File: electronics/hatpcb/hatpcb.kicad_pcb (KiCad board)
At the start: 2 copper layers, 72 x 60 mm, 4 parts, among them J1 Raspberry_Pi_GPIO, J2 encoder_1, J3 encoder_2, J4 Motor_Driver

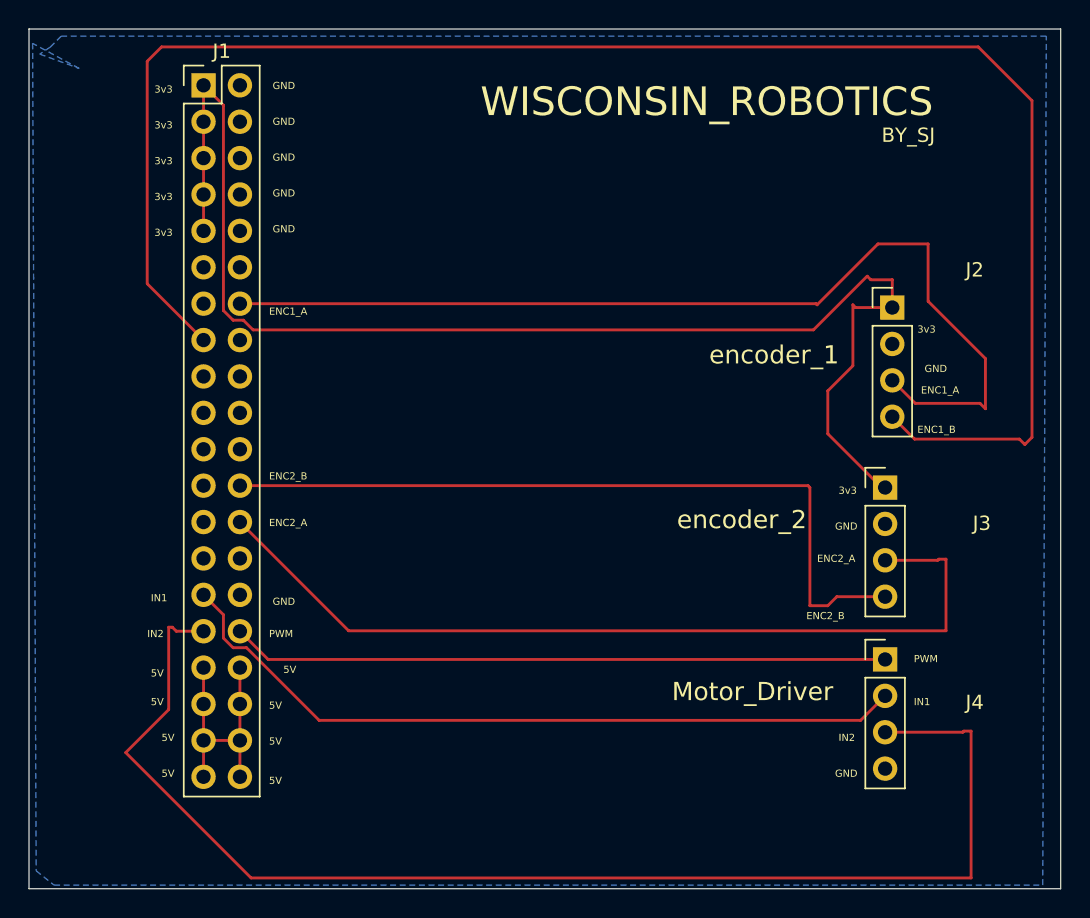
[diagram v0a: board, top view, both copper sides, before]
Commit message: Update hatpcb routing
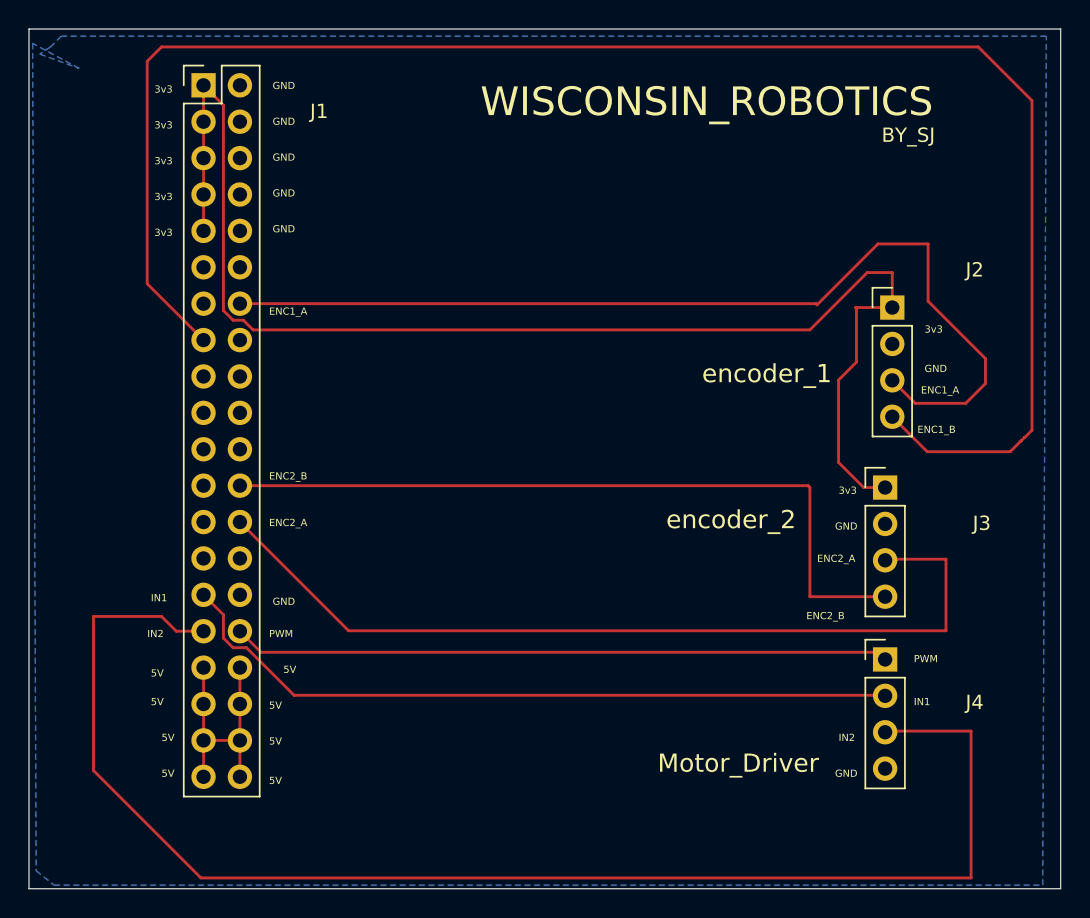
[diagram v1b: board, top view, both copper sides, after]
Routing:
- net /IN2: track 91.4 -> 99.5 mm
- net /IN1: track 52.9 -> 51.4 mm
- net /ENC1_A: track 70.3 -> 69.0 mm
- net /ENC2_B: track 53.6 -> 52.7 mm
